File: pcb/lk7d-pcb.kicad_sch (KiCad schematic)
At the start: 27 parts, among them J1 PINHD_1x4_Male, J2 PINHD_1x4_Male, SW1 RotaryEncoder_Switch_MP, SW2 RotaryEncoder_Switch_MP, SW3 SW_Push, SW4 SW_Push, SW5 SW_Push, SW6 SW_Push, SW7 SW_Push, SW8 SW_Push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

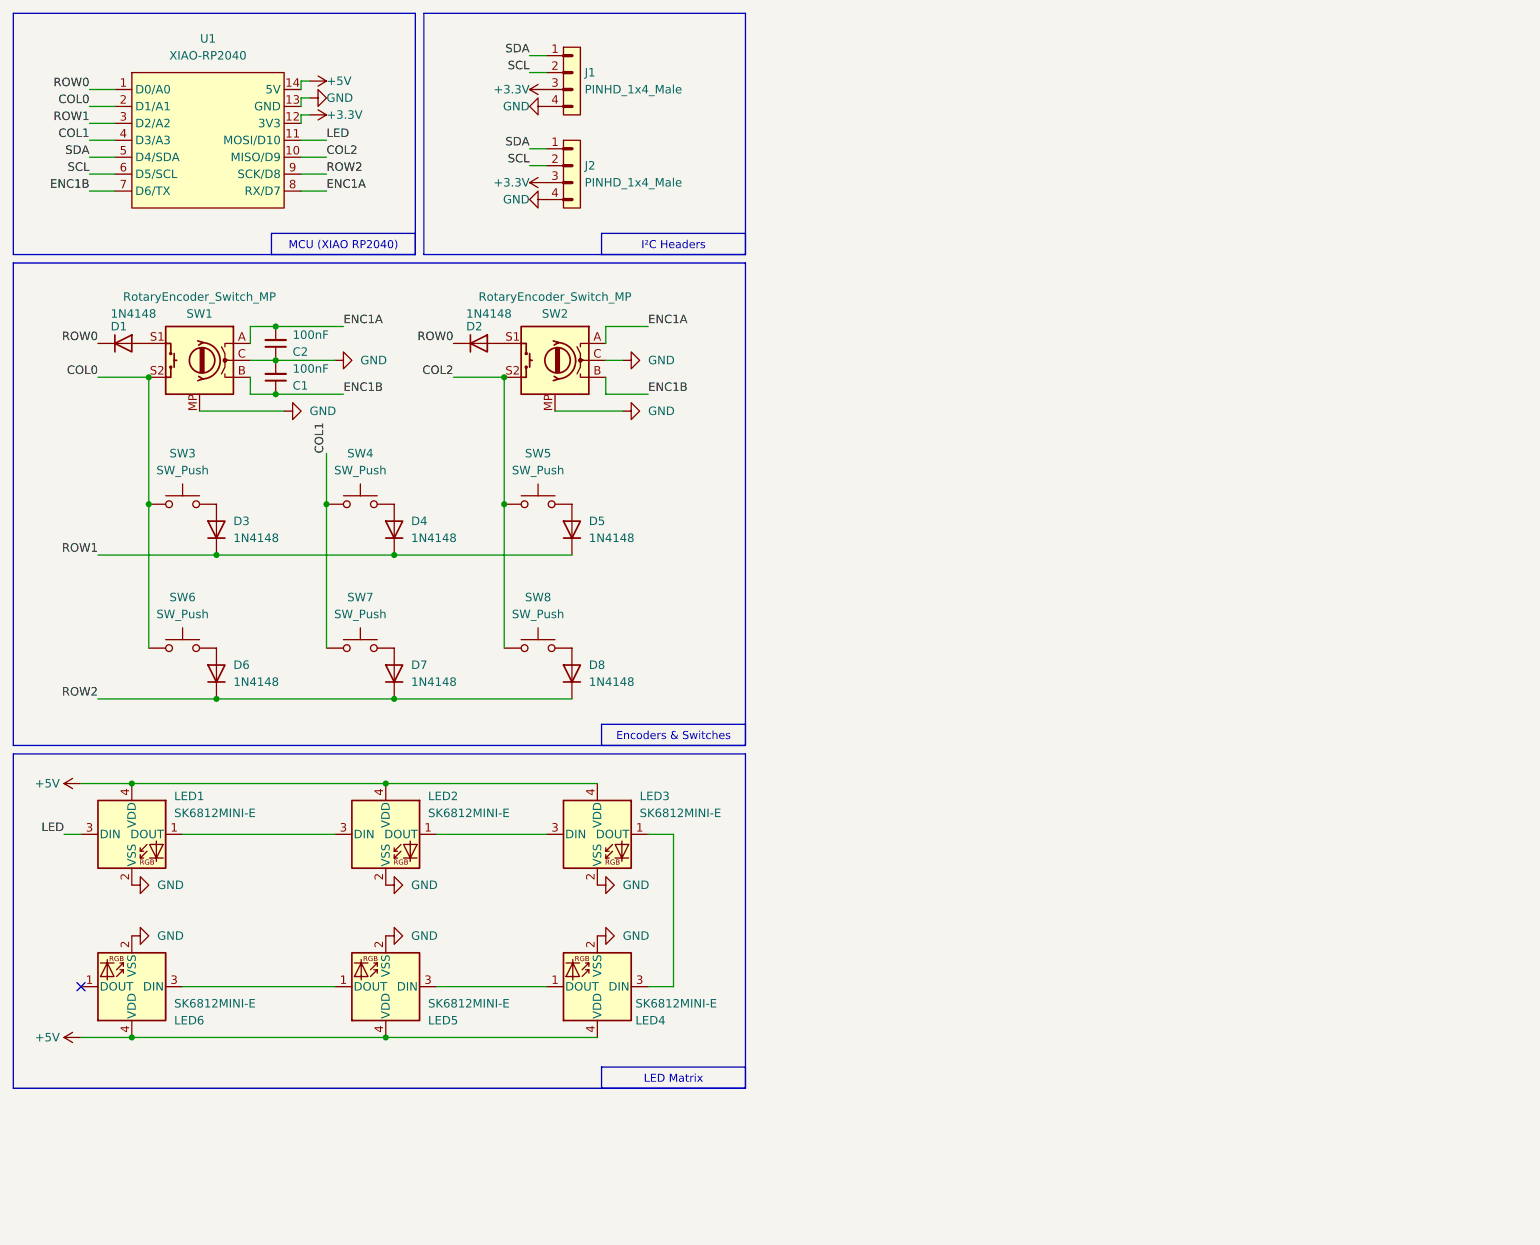
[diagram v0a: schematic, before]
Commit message: Add Logic Level Converter for per keys LEDs
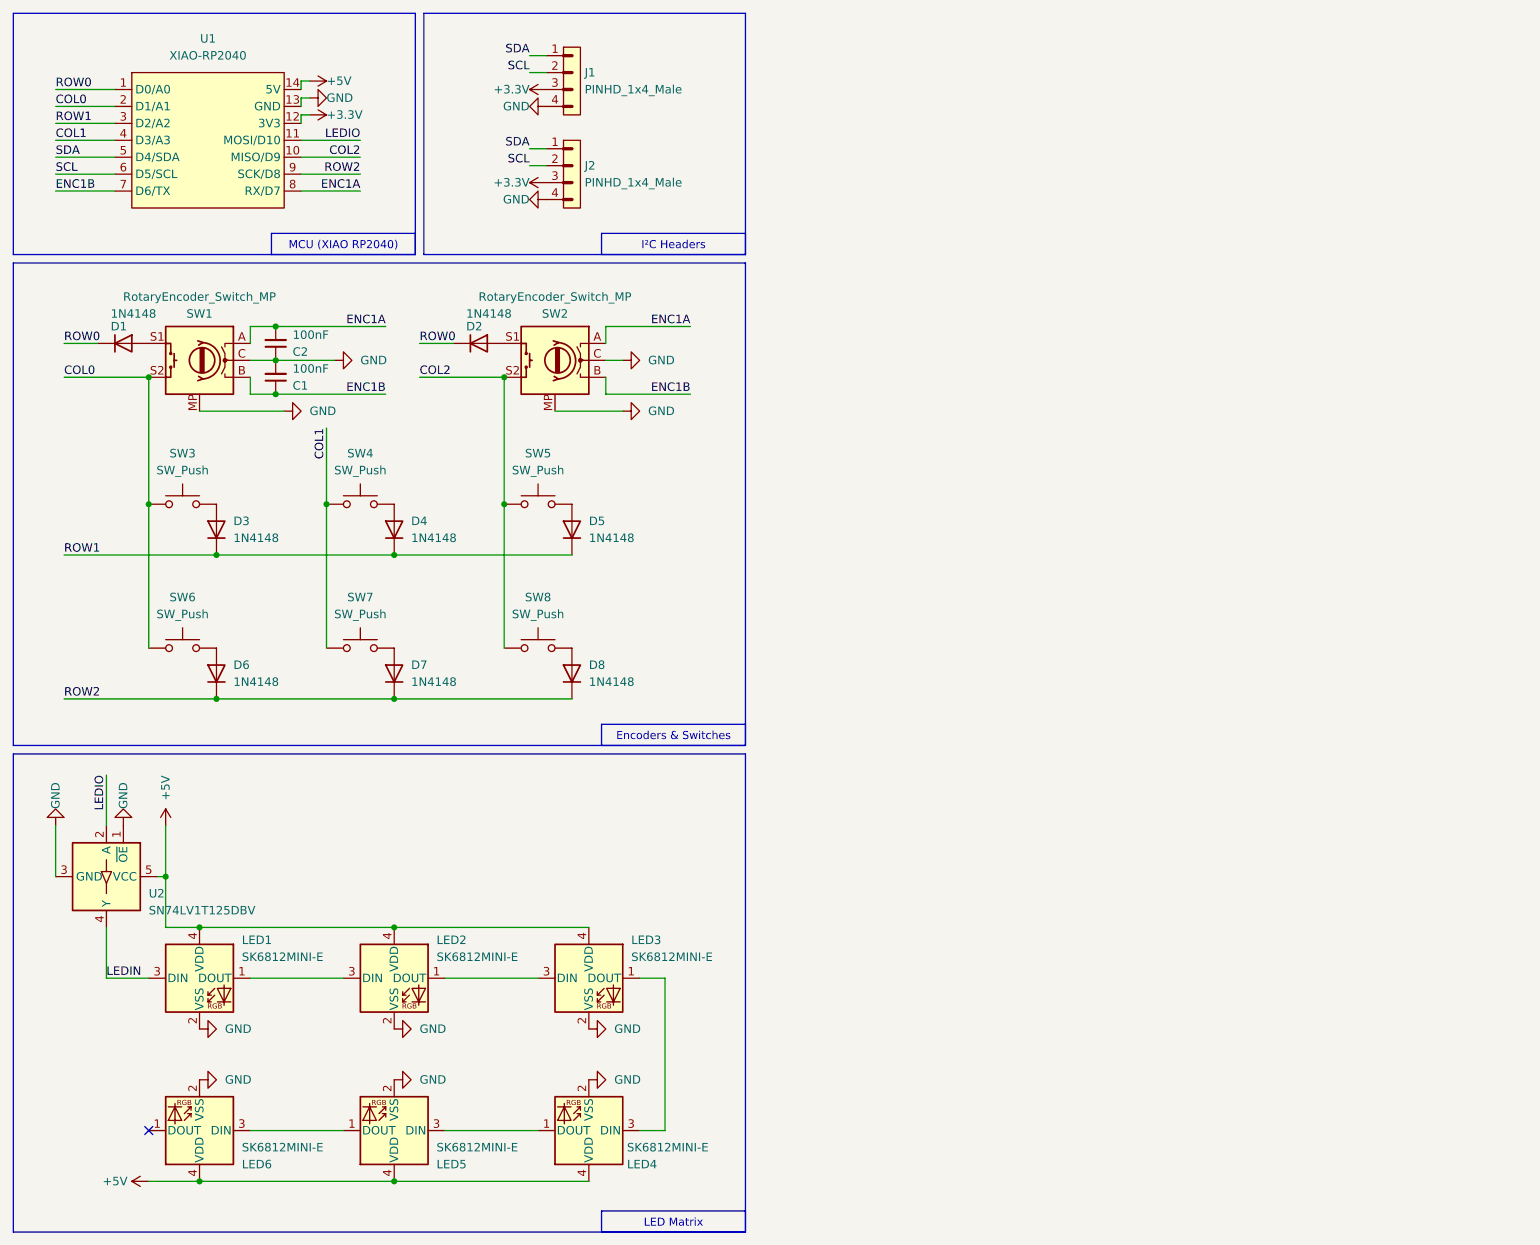
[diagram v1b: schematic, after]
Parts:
- added U2: SN74LV1T125DBV, Package_TO_SOT_SMD:SOT-23-5, symbol Logic_LevelTranslator:SN74LV1T125DBV
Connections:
- net +5V: now also U2.5 (VCC)
- net GND: now also U2.1 (~{OE}), U2.3 (GND)
- net LED renamed LEDIN
- net LEDIN: now also U2.4 (Y); no longer U1.11 (MOSI/D10)
- new net LEDIO: U1.11 (MOSI/D10), U2.2 (A)
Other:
- moved on the sheet: LED1, LED2, LED3, LED4, LED5, LED6

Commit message: Fix SK6812MINI-E pin mapping
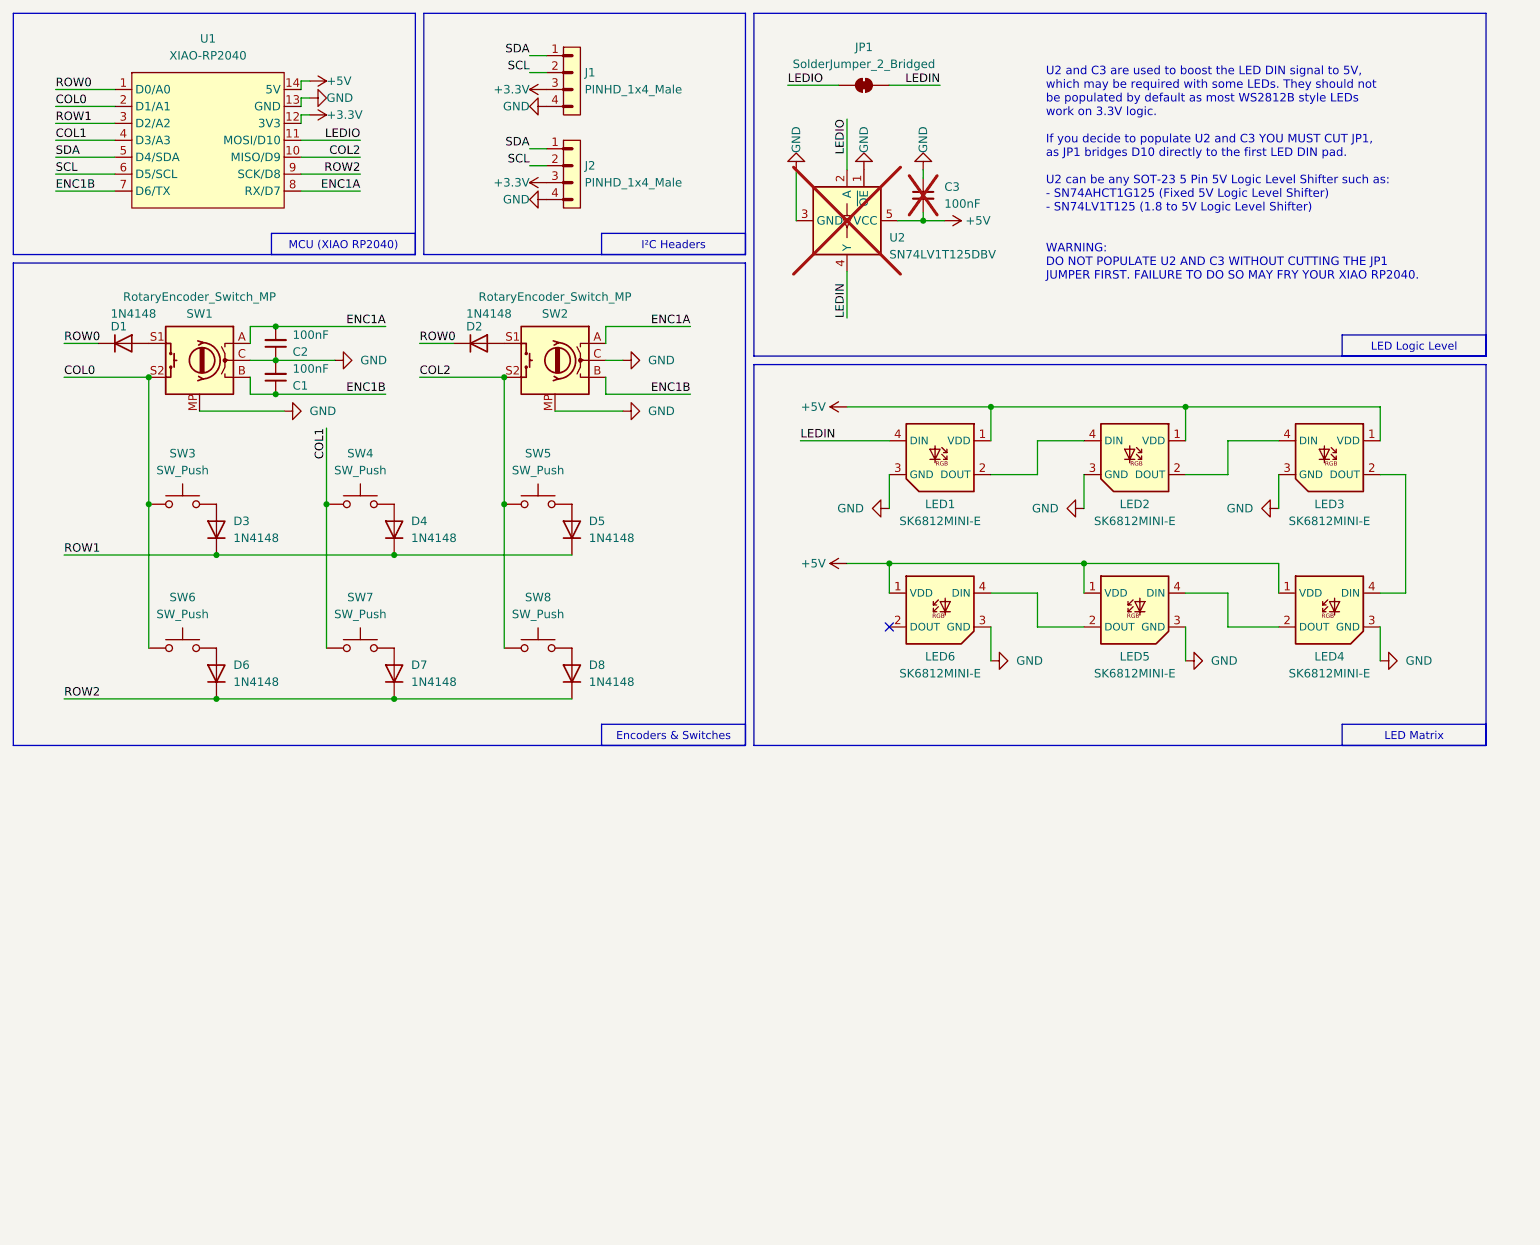
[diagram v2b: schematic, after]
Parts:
- removed LED1, LED2, LED3, LED4, LED5, LED6: SK6812MINI-E, LKBD_Common:LED_SK6812MINI-E, symbol LED:SK6812MINI
- added C3: 100nF, Capacitor_SMD:C_1206_3216Metric_Pad1.33x1.80mm_HandSolder, symbol Device:C_Small
- added JP1: SolderJumper_2_Bridged, Jumper:SolderJumper-2_P1.3mm_Bridged_RoundedPad1.0x1.5mm, symbol Jumper:SolderJumper_2_Bridged
- added LED1, LED2, LED3, LED4, LED5, LED6: SK6812MINI-E, LKBD_Common:LED_SK6812MINI-E, symbol LKBD_LED:SK6812MINI-E
- U2: now not fitted
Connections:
- net +5V: now also C3.2, LED1.1 (VDD), LED2.1 (VDD), LED3.1 (VDD), LED4.1 (VDD), LED5.1 (VDD), LED6.1 (VDD)
- net GND: now also C3.1, LED1.3 (GND), LED2.3 (GND), LED3.3 (GND), LED4.3 (GND), LED5.3 (GND), LED6.3 (GND)
- net LEDIN: now also JP1.2 (B), LED1.4 (DIN)
- net LEDIO: now also JP1.1 (A)
- new net: LED3.2 (DOUT), LED4.4 (DIN)
- new net: LED2.2 (DOUT), LED3.4 (DIN)
- new net: LED5.2 (DOUT), LED6.4 (DIN)
- new net: LED4.2 (DOUT), LED5.4 (DIN)
- new net: LED1.2 (DOUT), LED2.4 (DIN)
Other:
- note added: "LED Logic Level"
- note added: "U2 and C3 are used to boost the LED DIN signal to 5V, which may be required with some LEDs. They should not be populated by default as most WS2812B style LEDs work on 3.3V logic. If you decide to populate U2 and C3 YOU MUST CUT JP1, as JP1 bridges D10 directly to the first LED DIN pad. U2 can be any SOT-23 5 Pin 5V Logic Level Shifter such as: - SN74AHCT1G125 (Fixed 5V Logic Level Shifter) - SN74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"
